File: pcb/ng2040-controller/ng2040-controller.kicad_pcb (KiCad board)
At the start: 2 copper layers, 75 x 28 mm, 25 parts, among them J1 A, J2 B, J3 C, J4 D, J5 START, J6 SELECT, J7 JOY, J8 BATTERY, J9 NRF24L01 Connector, SW1 OPTS, SW2 POWER, U1 RP2040-Zero, U3 MIC5205-3.0YM5

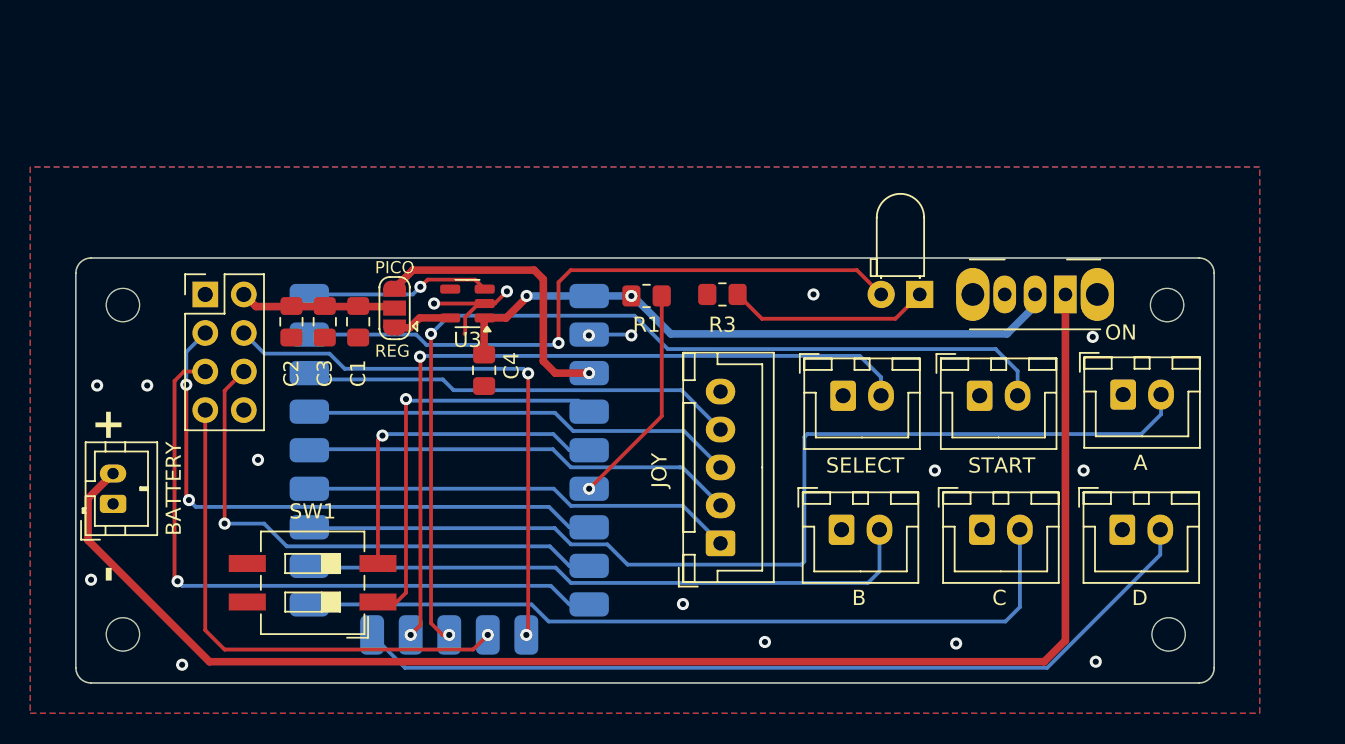
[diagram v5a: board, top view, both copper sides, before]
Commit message: Rerouting
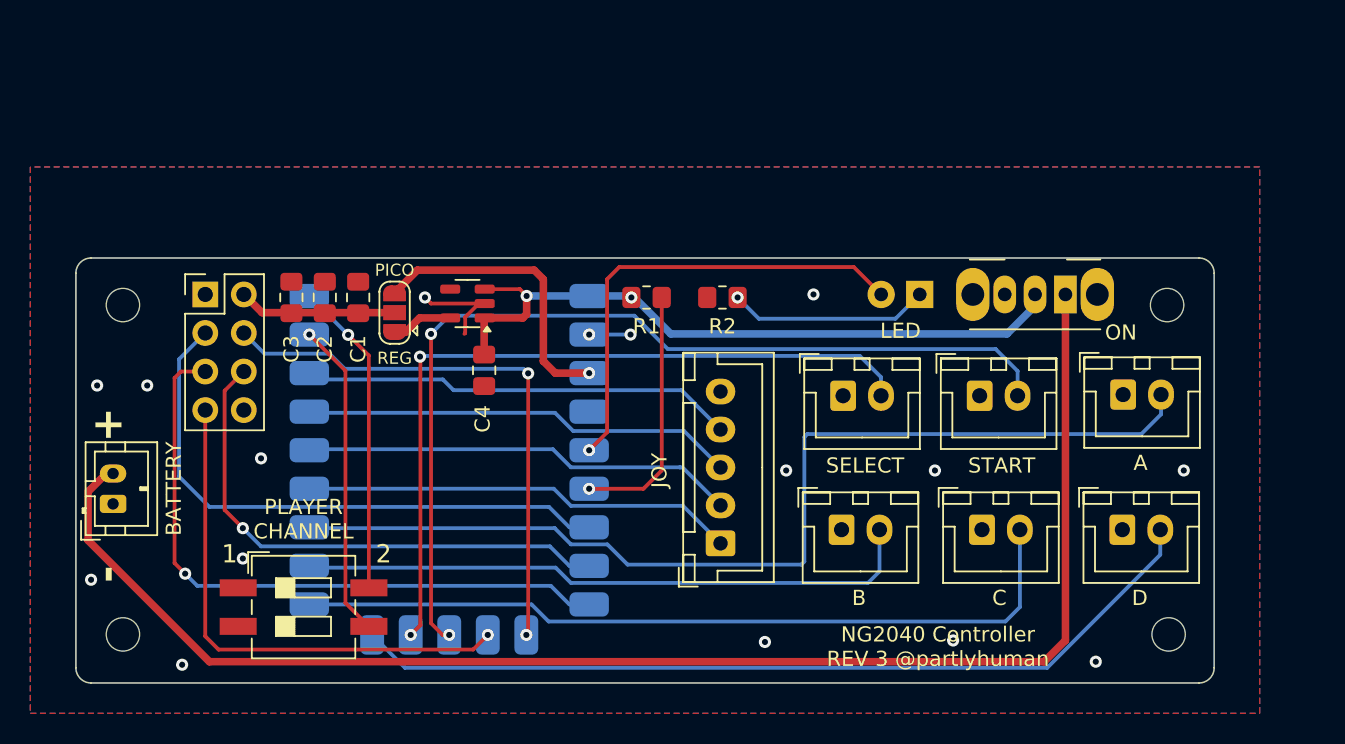
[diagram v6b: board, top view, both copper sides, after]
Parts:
- removed R3: 1K, Resistor_SMD:R_0805_2012Metric_Pad1.20x1.40mm_HandSolder
- added R2: 10K, Resistor_SMD:R_0805_2012Metric_Pad1.20x1.40mm_HandSolder, F.Cu at (80.6, 52.6)
- moved C2 2.72 mm to (54.4, 52.6), turned to -90 degrees
- moved C3 2.72 mm to (52.2, 52.6), turned to -90 degrees
- moved SW1 1.71 mm to (53.0, 73.0), turned to 0 degrees
- moved C1 1.60 mm to (56.6, 52.6), turned to -90 degrees
- moved JP1 0.30 mm to (59.0, 53.6)
- moved R1 0.10 mm to (75.6, 52.6)
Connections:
- SW1 pad 1: /SET_PLAYER -> GND
- SW1 pad 2: /SET_POWER -> GND
- SW1 pad 3: GND -> /SET_POWER
- SW1 pad 4: GND -> /SET_PLAYER
- U1 pad 1: /RADIO_EN -> /SET_PLAYER
- U1 pad 19: /SET_POWER -> /ACT_LED
- U1 pad 2: /ACT_LED -> /SET_POWER
- U1 pad 20: /SET_PLAYER -> unconnected-(U1-GP29-Pad20)
- U3 pad 3: /RADIO_EN -> /VIN
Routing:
- net /RADIO_EN: track 12.3 -> 0.00 mm, vias 1 -> 0
- net /ACT_LED: track 43.0 -> 30.9 mm
- net /SET_PLAYER: track 27.3 -> 21.0 mm
- net /VIN: track 41.9 -> 45.5 mm
- net /BAT_SENSE: track 14.7 -> 16.8 mm
- net GND: track 11.3 -> 9.96 mm, vias 17 -> 16
- net /SET_POWER: track 22.7 -> 21.5 mm
- net /MOSI: track 35.7 -> 35.2 mm
- net /CE: track 38.7 -> 38.6 mm, vias 2 -> 0
- net Net-(D1-K): track 13.3 -> 13.2 mm, vias 0 -> 1
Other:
- board text added: "${TITLE} REV ${REVISION} ${COMPANY}"
- board text added: "1"
- board text added: "2"
- board text added: "PLAYER CHANNEL"

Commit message: Committing to 3V reg, rewiring to use 3V reg to indirectly measure battery
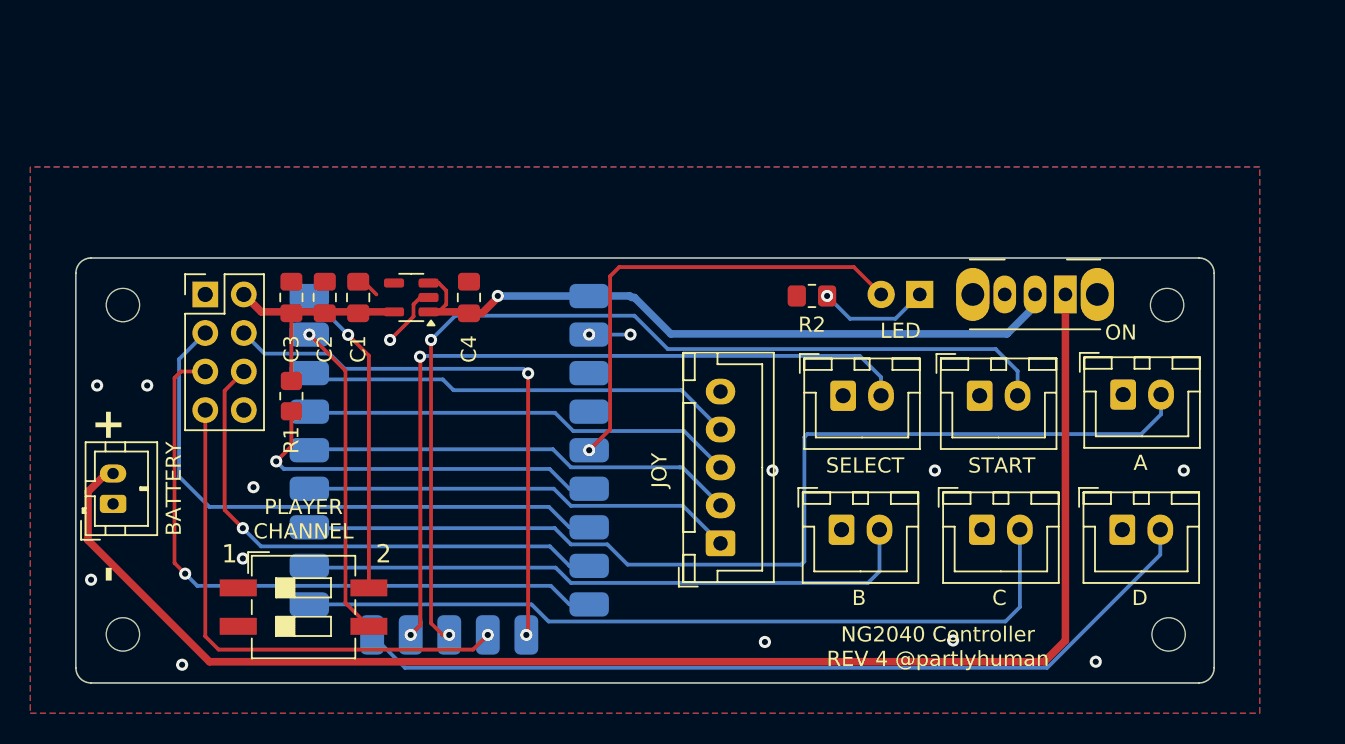
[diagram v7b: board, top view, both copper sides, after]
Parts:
- removed JP1: Radio PWR select, Jumper:SolderJumper-3_P1.3mm_Open_RoundedPad1.0x1.5mm
- moved R1 24.3 mm to (52.2, 59.1), turned to 90 degrees
- moved R2 5.90 mm to (86.5, 52.5)
- moved C4 4.90 mm to (63.9, 52.6), turned to -90 degrees
- moved U3 3.72 mm to (60.1, 52.6)
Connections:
- net /BAT_SENSE renamed Net-(U1-GP27)
- C1 pad 2: Net-(J9-Pin_2) -> /3V0
- C2 pad 2: Net-(J9-Pin_2) -> /3V0
- C3 pad 2: Net-(J9-Pin_2) -> /3V0
- J9 pad 2: Net-(J9-Pin_2) -> /3V0
- R1 pad 2: /VIN -> /3V0
- U1 pad 21: /3V3 -> unconnected-(U1-3V3-Pad21)
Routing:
- net /3V3: track 19.4 -> 0.00 mm, vias 1 -> 0
- net /3V0: track 4.06 -> 14.8 mm
- net Net-(J9-Pin_2): track 10.4 -> 0.00 mm
- net Net-(U1-GP27): track 16.8 -> 25.1 mm
- net Net-(D1-K): track 13.2 -> 7.38 mm
- net /VIN: track 45.5 -> 46.7 mm, vias 2 -> 1
- net GND: track 9.96 -> 8.78 mm, vias 16 -> 15
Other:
- board text removed: "PICO"
- board text removed: "REG"

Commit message: Minor noodling
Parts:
- J9: value NRF24L01 Connector -> RADIO
- U1: value RP2040-Zero -> RP2040 Tiny
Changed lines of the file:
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@@
 			(layer "F.Mask"
 				(type "Top Solder Mask")
+				(color "Black")
 				(thickness 0.01)
 			)
@@
 			(layer "B.Mask"
 				(type "Bottom Solder Mask")
+				(color "Black")
 				(thickness 0.01)
 			)
@@
 			)
 		)
-		(property "Value" "NRF24L01 Connector"
-			(at 1.27 9.95 0)
-			(layer "F.Fab")
+		(property "Value" "RADIO"
+			(at -2.225 4.1 90)
+			(layer "F.SilkS")
 			(effects
 				(font
@@
 			)
 		)
-		(property "Value" "RP2040-Zero"
+		(property "Value" "RP2040 Tiny"
 			(at 10.16 13.45 0)
 			(unlocked yes)
@@
 			(pintype "power_in")
 		)
-		(model "${KIPRJMOD}/Downloads/RP2040 Zero/RP2040_Zero.stp"
+		(model "${KIPRJMOD}/Downloads/RP2040-Tiny-Step_V1.1/RP2040-Tiny V1.1.step"
 			(offset
-				(xyz 1.2 0.8 2)
+				(xyz 1.2 0.8 1)
 			)
 			(scale
